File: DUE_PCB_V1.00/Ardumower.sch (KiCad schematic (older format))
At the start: 58 parts, among them J1 9V IN, J10 Sonar_R, J11 Sonar_C, J12 Sonar_L, J13 P_Right, J14 Buzzer, J15 Button, J16 US1, J17 US2, J18 US3, J19 P_Left, J2 I2C0_1, J20 Remote, J21 PCB_2, J22 Ser0, J23 Ser1, J24 Ser2, J25 5V IN, J29 3.3V IN, J3 I2C0_2, J30 I2C1_2, J31 Ser3, J33 ReserveD8, J34 ReserveD9, J35 ReserveD49, J36 ReserveA10, J4 I2C1_1, J5 Bumper, J6 Drop, J8 Tilt, J9 Rain

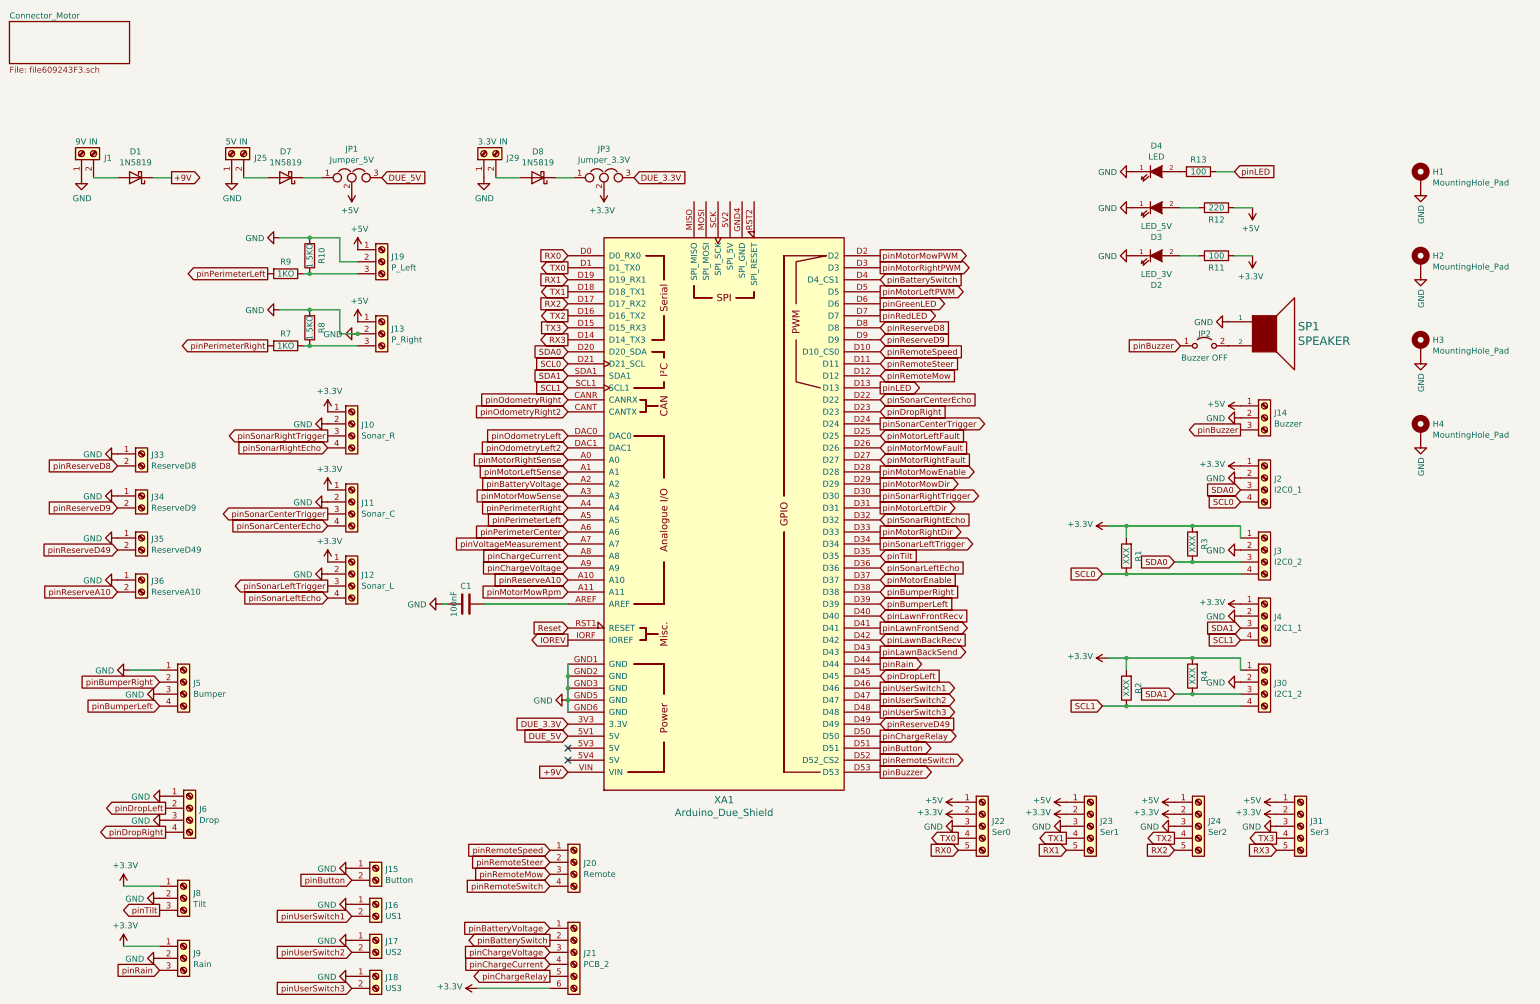
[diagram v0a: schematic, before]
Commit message: New Pins added
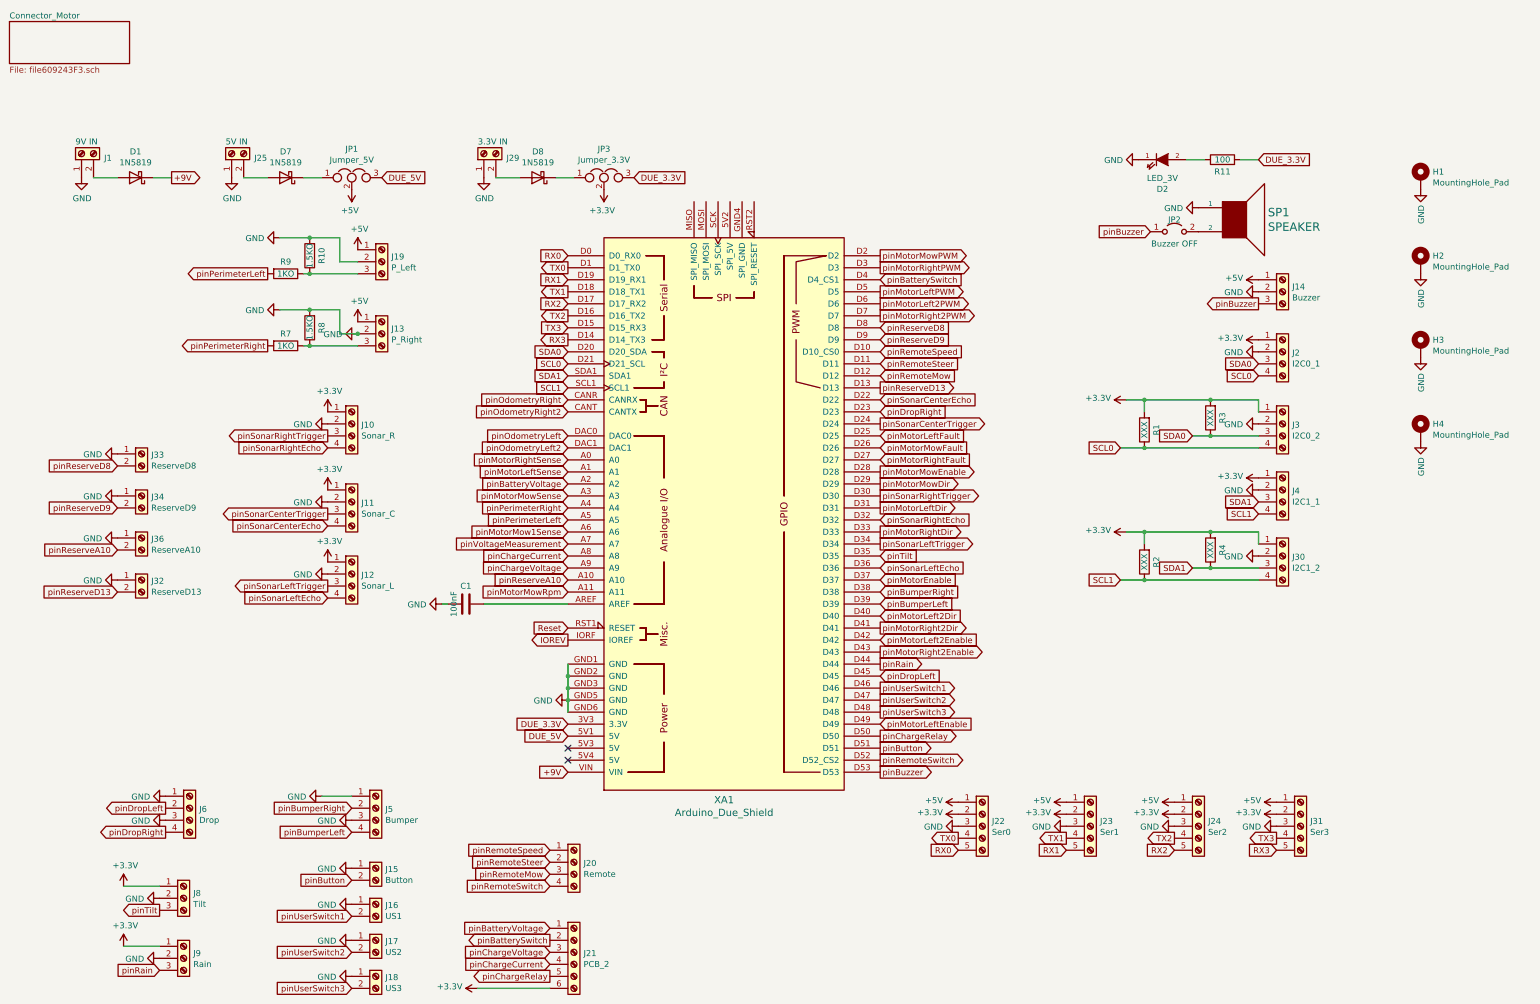
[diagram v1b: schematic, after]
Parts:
- removed D3: LED_5V, LED_THT:LED_D3.0mm, symbol Zimprich:LED
- removed D4: LED, LED_THT:LED_D3.0mm, symbol Zimprich:LED
- removed J35: ReserveD49, Connector_PinHeader_2.54mm:PinHeader_1x02_P2.54mm_Vertical, symbol Connector:Screw_Terminal_01x02
- removed R12: 220, Resistor_THT:R_Axial_DIN0207_L6.3mm_D2.5mm_P2.54mm_Vertical, symbol Device:R
- removed R13: 100, Resistor_THT:R_Axial_DIN0207_L6.3mm_D2.5mm_P2.54mm_Vertical, symbol Device:R
- added J32: ReserveD13, Connector_PinHeader_2.54mm:PinHeader_1x02_P2.54mm_Vertical, symbol Connector:Screw_Terminal_01x02
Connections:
- net +3V3: no longer R11.2
- net DUE_3.3V: now also R11.2
- net GND: now also J32.1 (Pin_1)
- net pinGreenLED renamed pinMotorLeft2PWM
- net pinLED renamed pinReserveD13
- net pinReserveD13: now also J32.2 (Pin_2)
- net pinLawnBackRecv renamed pinMotorLeft2Enable
- net pinLawnBackSend renamed pinMotorRight2Enable
- net pinLawnFrontRecv renamed pinMotorLeft2Dir
- net pinLawnFrontSend renamed pinMotorRight2Dir
- net pinPerimeterCenter renamed pinMotorMow1Sense
- net pinRedLED renamed pinMotorRight2PWM
- net pinReserveD49 renamed pinMotorLeftEnable
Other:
- moved on the sheet: D2, J14, J2, J3, J30, J36, J4, J5, JP2, R1, R11, R2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

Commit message: Change to JST-XH
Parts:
- J10, J11, J12, J2, J20, J3, J30, J4, J5, J6: footprint Connector_PinHeader_2.54mm:PinHeader_1x04_P2.54mm_Vertical -> Connector_JST:JST_XH_B4B-XH-A_1x04_P2.50mm_Vertical
- J13, J14, J19, J8, J9: footprint Connector_PinHeader_2.54mm:PinHeader_1x03_P2.54mm_Vertical -> Connector_JST:JST_XH_B3B-XH-A_1x03_P2.50mm_Vertical
- J15, J16, J17, J18, J32, J33, J34, J36: footprint Connector_PinHeader_2.54mm:PinHeader_1x02_P2.54mm_Vertical -> Connector_JST:JST_XH_B2B-XH-A_1x02_P2.50mm_Vertical
- J21: footprint Connector_PinHeader_2.54mm:PinHeader_1x06_P2.54mm_Vertical -> Connector_JST:JST_XH_B6B-XH-A_1x06_P2.50mm_Vertical
- J22, J23, J24, J31: footprint Connector_PinHeader_2.54mm:PinHeader_1x05_P2.54mm_Vertical -> Connector_JST:JST_XH_B5B-XH-A_1x05_P2.50mm_Vertical
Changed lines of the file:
@@
 F 0 "J10" H 3130 2892 50  0000 L CNN
 F 1 "Sonar_R" H 3130 2801 50  0000 L CNN
-F 2 "Connector_PinHeader_2.54mm:PinHeader_1x04_P2.54mm_Vertical" H 3050 2900 50  0001 C CNN
+F 2 "Connector_JST:JST_XH_B4B-XH-A_1x04_P2.50mm_Vertical" H 3050 2900 50  0001 C CNN
 F 3 "~" H 3050 2900 50  0001 C CNN
 	1    3050 2900
@@
 F 0 "J11" H 3130 3542 50  0000 L CNN
 F 1 "Sonar_C" H 3130 3451 50  0000 L CNN
-F 2 "Connector_PinHeader_2.54mm:PinHeader_1x04_P2.54mm_Vertical" H 3050 3550 50  0001 C CNN
+F 2 "Connector_JST:JST_XH_B4B-XH-A_1x04_P2.50mm_Vertical" H 3050 3550 50  0001 C CNN
 F 3 "~" H 3050 3550 50  0001 C CNN
 	1    3050 3550
@@
 F 0 "J12" H 3130 4142 50  0000 L CNN
 F 1 "Sonar_L" H 3130 4051 50  0000 L CNN
-F 2 "Connector_PinHeader_2.54mm:PinHeader_1x04_P2.54mm_Vertical" H 3050 4150 50  0001 C CNN
+F 2 "Connector_JST:JST_XH_B4B-XH-A_1x04_P2.50mm_Vertical" H 3050 4150 50  0001 C CNN
 F 3 "~" H 3050 4150 50  0001 C CNN
 	1    3050 4150
@@
 F 0 "J5" H 3330 6092 50  0000 L CNN
 F 1 "Bumper" H 3330 6001 50  0000 L CNN
-F 2 "Connector_PinHeader_2.54mm:PinHeader_1x04_P2.54mm_Vertical" H 3250 6100 50  0001 C CNN
+F 2 "Connector_JST:JST_XH_B4B-XH-A_1x04_P2.50mm_Vertical" H 3250 6100 50  0001 C CNN
 F 3 "~" H 3250 6100 50  0001 C CNN
 	1    3250 6100
@@
 F 0 "J19" H 3380 1592 50  0000 L CNN
 F 1 "P_Left" H 3380 1501 50  0000 L CNN
-F 2 "Connector_PinHeader_2.54mm:PinHeader_1x03_P2.54mm_Vertical" H 3300 1550 50  0001 C CNN
+F 2 "Connector_JST:JST_XH_B3B-XH-A_1x03_P2.50mm_Vertical" H 3300 1550 50  0001 C CNN
 F 3 "~" H 3300 1550 50  0001 C CNN
 	1    3300 1550
@@
 F 0 "J13" H 3380 2192 50  0000 L CNN
 F 1 "P_Right" H 3380 2101 50  0000 L CNN
-F 2 "Connector_PinHeader_2.54mm:PinHeader_1x03_P2.54mm_Vertical" H 3300 2150 50  0001 C CNN
+F 2 "Connector_JST:JST_XH_B3B-XH-A_1x03_P2.50mm_Vertical" H 3300 2150 50  0001 C CNN
 F 3 "~" H 3300 2150 50  0001 C CNN
 	1    3300 2150
@@
 F 0 "J8" H 1730 6892 50  0000 L CNN
 F 1 "Tilt" H 1730 6801 50  0000 L CNN
-F 2 "Connector_PinHeader_2.54mm:PinHeader_1x03_P2.54mm_Vertical" H 1650 6850 50  0001 C CNN
+F 2 "Connector_JST:JST_XH_B3B-XH-A_1x03_P2.50mm_Vertical" H 1650 6850 50  0001 C CNN
 F 3 "~" H 1650 6850 50  0001 C CNN
 	1    1650 6850
@@
 F 0 "J9" H 1730 7392 50  0000 L CNN
 F 1 "Rain" H 1730 7301 50  0000 L CNN
-F 2 "Connector_PinHeader_2.54mm:PinHeader_1x03_P2.54mm_Vertical" H 1650 7350 50  0001 C CNN
+F 2 "Connector_JST:JST_XH_B3B-XH-A_1x03_P2.50mm_Vertical" H 1650 7350 50  0001 C CNN
 F 3 "~" H 1650 7350 50  0001 C CNN
 	1    1650 7350
@@
 F 0 "J15" H 3330 6592 50  0000 L CNN
 F 1 "Button" H 3330 6501 50  0000 L CNN
-F 2 "Connector_PinHeader_2.54mm:PinHeader_1x02_P2.54mm_Vertical" H 3250 6600 50  0001 C CNN
+F 2 "Connector_JST:JST_XH_B2B-XH-A_1x02_P2.50mm_Vertical" H 3250 6600 50  0001 C CNN
 F 3 "~" H 3250 6600 50  0001 C CNN
 	1    3250 6600
@@
 F 0 "J21" H 4980 7292 50  0000 L CNN
 F 1 "PCB_2" H 4980 7201 50  0000 L CNN
-F 2 "Connector_PinHeader_2.54mm:PinHeader_1x06_P2.54mm_Vertical" H 4900 7300 50  0001 C CNN
+F 2 "Connector_JST:JST_XH_B6B-XH-A_1x06_P2.50mm_Vertical" H 4900 7300 50  0001 C CNN
 F 3 "~" H 4900 7300 50  0001 C CNN
 	1    4900 7300
@@
 F 0 "J20" H 4980 6542 50  0000 L CNN
 F 1 "Remote" H 4980 6451 50  0000 L CNN
-F 2 "Connector_PinHeader_2.54mm:PinHeader_1x04_P2.54mm_Vertical" H 4900 6550 50  0001 C CNN
+F 2 "Connector_JST:JST_XH_B4B-XH-A_1x04_P2.50mm_Vertical" H 4900 6550 50  0001 C CNN
 F 3 "~" H 4900 6550 50  0001 C CNN
 	1    4900 6550
@@
 F 0 "J16" H 3330 6892 50  0000 L CNN
 F 1 "US1" H 3330 6801 50  0000 L CNN
-F 2 "Connector_PinHeader_2.54mm:PinHeader_1x02_P2.54mm_Vertical" H 3250 6900 50  0001 C CNN
+F 2 "Connector_JST:JST_XH_B2B-XH-A_1x02_P2.50mm_Vertical" H 3250 6900 50  0001 C CNN
 F 3 "~" H 3250 6900 50  0001 C CNN
 	1    3250 6900
@@
 F 0 "J17" H 3330 7192 50  0000 L CNN
 F 1 "US2" H 3330 7101 50  0000 L CNN
-F 2 "Connector_PinHeader_2.54mm:PinHeader_1x02_P2.54mm_Vertical" H 3250 7200 50  0001 C CNN
+F 2 "Connector_JST:JST_XH_B2B-XH-A_1x02_P2.50mm_Vertical" H 3250 7200 50  0001 C CNN
 F 3 "~" H 3250 7200 50  0001 C CNN
 	1    3250 7200
@@
 F 0 "J18" H 3330 7492 50  0000 L CNN
 F 1 "US3" H 3330 7401 50  0000 L CNN
-F 2 "Connector_PinHeader_2.54mm:PinHeader_1x02_P2.54mm_Vertical" H 3250 7500 50  0001 C CNN
+F 2 "Connector_JST:JST_XH_B2B-XH-A_1x02_P2.50mm_Vertical" H 3250 7500 50  0001 C CNN
 F 3 "~" H 3250 7500 50  0001 C CNN
 	1    3250 7500
@@
 F 0 "J14" H 10880 1842 50  0000 L CNN
 F 1 "Buzzer" H 10880 1751 50  0000 L CNN
-F 2 "Connector_PinHeader_2.54mm:PinHeader_1x03_P2.54mm_Vertical" H 10800 1800 50  0001 C CNN
+F 2 "Connector_JST:JST_XH_B3B-XH-A_1x03_P2.50mm_Vertical" H 10800 1800 50  0001 C CNN
 F 3 "~" H 10800 1800 50  0001 C CNN
 	1    10800 1800
@@
 F 0 "J2" H 10880 2292 50  0000 L CNN
 F 1 "I2C0_1" H 10880 2201 50  0000 L CNN
-F 2 "Connector_PinHeader_2.54mm:PinHeader_1x04_P2.54mm_Vertical" H 10800 2300 50  0001 C CNN
+F 2 "Connector_JST:JST_XH_B4B-XH-A_1x04_P2.50mm_Vertical" H 10800 2300 50  0001 C CNN
 F 3 "~" H 10800 2300 50  0001 C CNN
 	1    10800 2300
@@
 F 0 "J3" H 10880 2892 50  0000 L CNN
 F 1 "I2C0_2" H 10880 2801 50  0000 L CNN
-F 2 "Connector_PinHeader_2.54mm:PinHeader_1x04_P2.54mm_Vertical" H 10800 2900 50  0001 C CNN
+F 2 "Connector_JST:JST_XH_B4B-XH-A_1x04_P2.50mm_Vertical" H 10800 2900 50  0001 C CNN
 F 3 "~" H 10800 2900 50  0001 C CNN
 	1    10800 2900
@@
 F 0 "J4" H 10880 3442 50  0000 L CNN
 F 1 "I2C1_1" H 10880 3351 50  0000 L CNN
-F 2 "Connector_PinHeader_2.54mm:PinHeader_1x04_P2.54mm_Vertical" H 10800 3450 50  0001 C CNN
+F 2 "Connector_JST:JST_XH_B4B-XH-A_1x04_P2.50mm_Vertical" H 10800 3450 50  0001 C CNN
 F 3 "~" H 10800 3450 50  0001 C CNN
 	1    10800 3450
@@
 F 0 "J30" H 10880 3992 50  0000 L CNN
 F 1 "I2C1_2" H 10880 3901 50  0000 L CNN
-F 2 "Connector_PinHeader_2.54mm:PinHeader_1x04_P2.54mm_Vertical" H 10800 4000 50  0001 C CNN
+F 2 "Connector_JST:JST_XH_B4B-XH-A_1x04_P2.50mm_Vertical" H 10800 4000 50  0001 C CNN
 F 3 "~" H 10800 4000 50  0001 C CNN
 	1    10800 4000
@@
 F 0 "J23" H 9280 6292 50  0000 L CNN
 F 1 "Ser1" H 9280 6201 50  0000 L CNN
-F 2 "Connector_PinHeader_2.54mm:PinHeader_1x05_P2.54mm_Vertical" H 9200 6250 50  0001 C CNN
+F 2 "Connector_JST:JST_XH_B5B-XH-A_1x05_P2.50mm_Vertical" H 9200 6250 50  0001 C CNN
 F 3 "~" H 9200 6250 50  0001 C CNN
 	1    9200 6250
@@
 F 0 "J24" H 10180 6292 50  0000 L CNN
 F 1 "Ser2" H 10180 6201 50  0000 L CNN
-F 2 "Connector_PinHeader_2.54mm:PinHeader_1x05_P2.54mm_Vertical" H 10100 6250 50  0001 C CNN
+F 2 "Connector_JST:JST_XH_B5B-XH-A_1x05_P2.50mm_Vertical" H 10100 6250 50  0001 C CNN
 F 3 "~" H 10100 6250 50  0001 C CNN
 	1    10100 6250
@@
 F 0 "J22" H 8380 6292 50  0000 L CNN
 F 1 "Ser0" H 8380 6201 50  0000 L CNN
-F 2 "Connector_PinHeader_2.54mm:PinHeader_1x05_P2.54mm_Vertical" H 8300 6250 50  0001 C CNN
+F 2 "Connector_JST:JST_XH_B5B-XH-A_1x05_P2.50mm_Vertical" H 8300 6250 50  0001 C CNN
 F 3 "~" H 8300 6250 50  0001 C CNN
 	1    8300 6250
@@
 F 0 "J31" H 11030 6292 50  0000 L CNN
 F 1 "Ser3" H 11030 6201 50  0000 L CNN
-F 2 "Connector_PinHeader_2.54mm:PinHeader_1x05_P2.54mm_Vertical" H 10950 6250 50  0001 C CNN
+F 2 "Connector_JST:JST_XH_B5B-XH-A_1x05_P2.50mm_Vertical" H 10950 6250 50  0001 C CNN
 F 3 "~" H 10950 6250 50  0001 C CNN
 	1    10950 6250
@@
 F 0 "J33" H 1380 3142 50  0000 L CNN
 F 1 "ReserveD8" H 1380 3051 50  0000 L CNN
-F 2 "Connector_PinHeader_2.54mm:PinHeader_1x02_P2.54mm_Vertical" H 1300 3150 50  0001 C CNN
+F 2 "Connector_JST:JST_XH_B2B-XH-A_1x02_P2.50mm_Vertical" H 1300 3150 50  0001 C CNN
 F 3 "~" H 1300 3150 50  0001 C CNN
 	1    1300 3150
@@
 F 0 "J34" H 1380 3492 50  0000 L CNN
 F 1 "ReserveD9" H 1380 3401 50  0000 L CNN
-F 2 "Connector_PinHeader_2.54mm:PinHeader_1x02_P2.54mm_Vertical" H 1300 3500 50  0001 C CNN
+F 2 "Connector_JST:JST_XH_B2B-XH-A_1x02_P2.50mm_Vertical" H 1300 3500 50  0001 C CNN
 F 3 "~" H 1300 3500 50  0001 C CNN
 	1    1300 3500
@@
 F 0 "J36" H 1380 3842 50  0000 L CNN
 F 1 "ReserveA10" H 1380 3751 50  0000 L CNN
-F 2 "Connector_PinHeader_2.54mm:PinHeader_1x02_P2.54mm_Vertical" H 1300 3850 50  0001 C CNN
+F 2 "Connector_JST:JST_XH_B2B-XH-A_1x02_P2.50mm_Vertical" H 1300 3850 50  0001 C CNN
 F 3 "~" H 1300 3850 50  0001 C CNN
 	1    1300 3850
@@
 F 0 "J6" H 1780 6092 50  0000 L CNN
 F 1 "Drop" H 1780 6001 50  0000 L CNN
-F 2 "Connector_PinHeader_2.54mm:PinHeader_1x04_P2.54mm_Vertical" H 1700 6100 50  0001 C CNN
+F 2 "Connector_JST:JST_XH_B4B-XH-A_1x04_P2.50mm_Vertical" H 1700 6100 50  0001 C CNN
 F 3 "~" H 1700 6100 50  0001 C CNN
 	1    1700 6100
@@
 F 0 "J32" H 1380 4192 50  0000 L CNN
 F 1 "ReserveD13" H 1380 4101 50  0000 L CNN
-F 2 "Connector_PinHeader_2.54mm:PinHeader_1x02_P2.54mm_Vertical" H 1300 4200 50  0001 C CNN
+F 2 "Connector_JST:JST_XH_B2B-XH-A_1x02_P2.50mm_Vertical" H 1300 4200 50  0001 C CNN
 F 3 "~" H 1300 4200 50  0001 C CNN
 	1    1300 4200

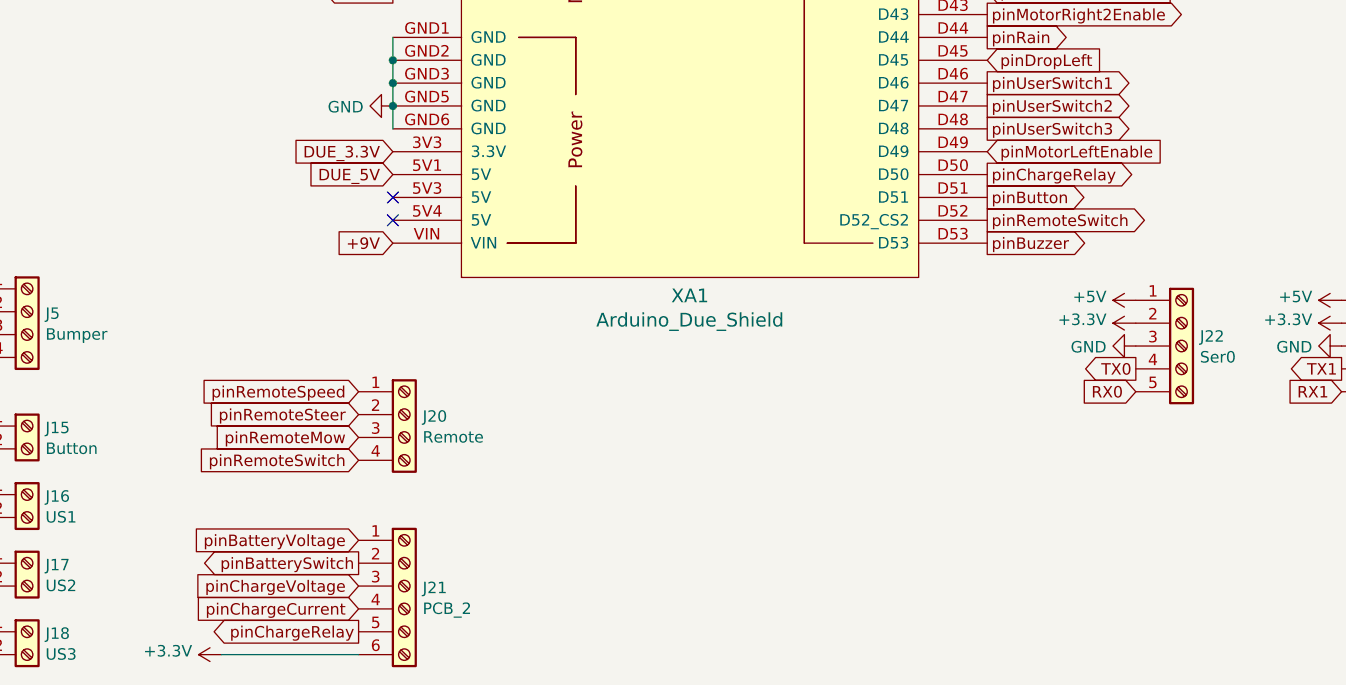
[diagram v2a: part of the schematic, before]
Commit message: Rename pinChargeRelay to pinChargeEnable
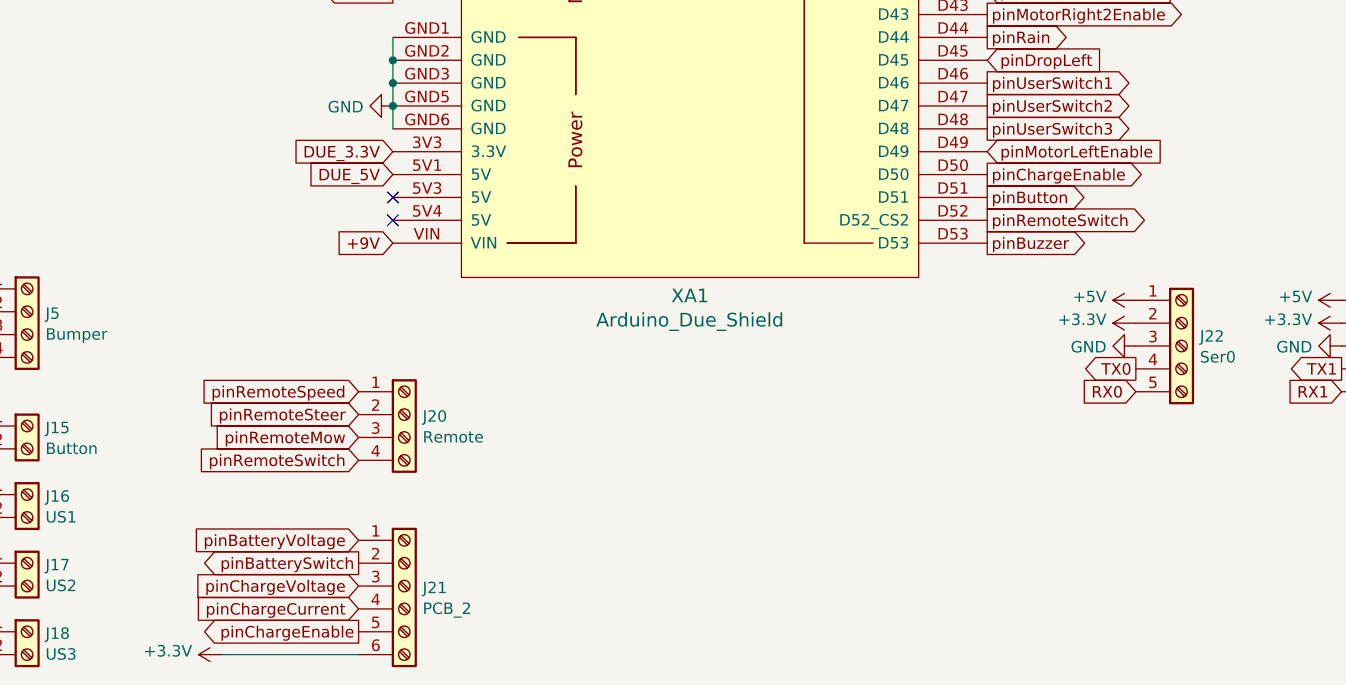
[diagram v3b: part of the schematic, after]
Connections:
- net pinChargeRelay renamed pinChargeEnable
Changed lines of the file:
@@
 pinChargeCurrent
 Text GLabel 7450 5500 2    50   Output ~ 0
-pinChargeRelay
+pinChargeEnable
 Text GLabel 7450 2500 2    50   Input ~ 0
 pinRemoteMow
@@
 pinChargeCurrent
 Text GLabel 4700 7500 0    50   Output ~ 0
-pinChargeRelay
+pinChargeEnable
 $Comp
 L Connector:Screw_Terminal_01x04 J20

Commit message: PCB ODO Names Changes
Change ODO LEFT to Right. Create new Schematic PDF. Create New Gerber Files.
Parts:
- D2: symbol Zimprich:LED -> Ardumower-rescue:LED-Zimprich
- SP1: symbol Lötpad_2,5mm:SPEAKER -> Ardumower-rescue:SPEAKER-Lötpad_2,5mm
- XA1: symbol arduino:Arduino_Due_Shield -> Ardumower-rescue:Arduino_Due_Shield-arduino
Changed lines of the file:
@@
 Connection ~ 4850 5000
 $Comp
-L arduino:Arduino_Due_Shield XA1
+L Ardumower-rescue:Arduino_Due_Shield-arduino XA1
 U 1 1 606B55C4
 P 6150 3650
@@
 $EndComp
 $Comp
-L Zimprich:LED D2
+L Ardumower-rescue:LED-Zimprich D2
 U 1 1 608BB0E1
 P 9800 700
@@
 $EndComp
 $Comp
-L Lötpad_2,5mm:SPEAKER SP1
+L Ardumower-rescue:SPEAKER-Lötpad_2,5mm SP1
 U 1 1 607B6900
 P 10400 1200
